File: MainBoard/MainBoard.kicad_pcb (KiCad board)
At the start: 6 copper layers, 45 x 44 mm, 110 parts, among them J2 USB4110-GF-A, J3 M55-7104042R, J4 Conn_01x04_Pin, J5 Conn_01x02_Pin, Q1 PMV19XNEAR, Q2 PMV19XNEAR, Q3 PMV19XNEAR, Q4 PMV19XNEAR, SW1 SW_TL1015AF160QG, SW2 SW_TL1015AF160QG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

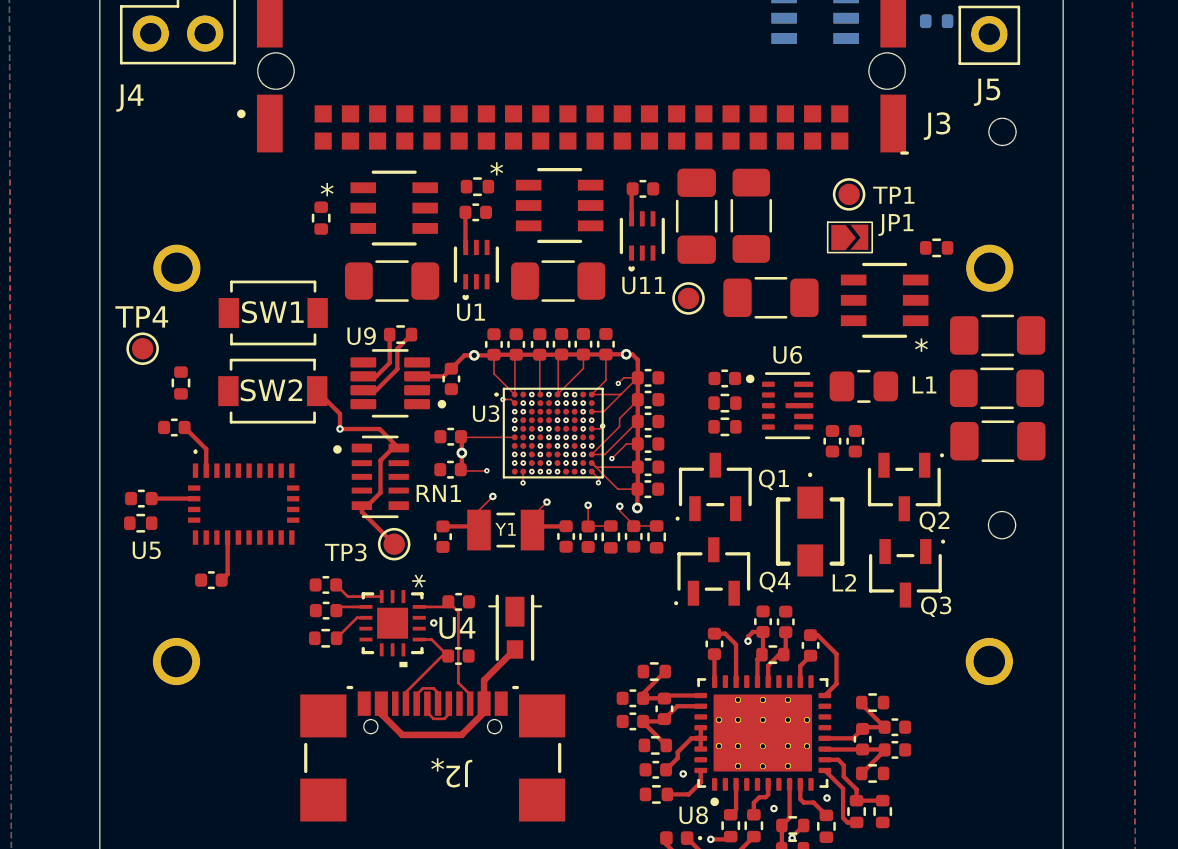
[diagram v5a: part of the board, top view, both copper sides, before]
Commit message: Routed a bunch of stuff
Most if not all fill zones are done
Most if not all cap to 3.3V are done
To start working on communication
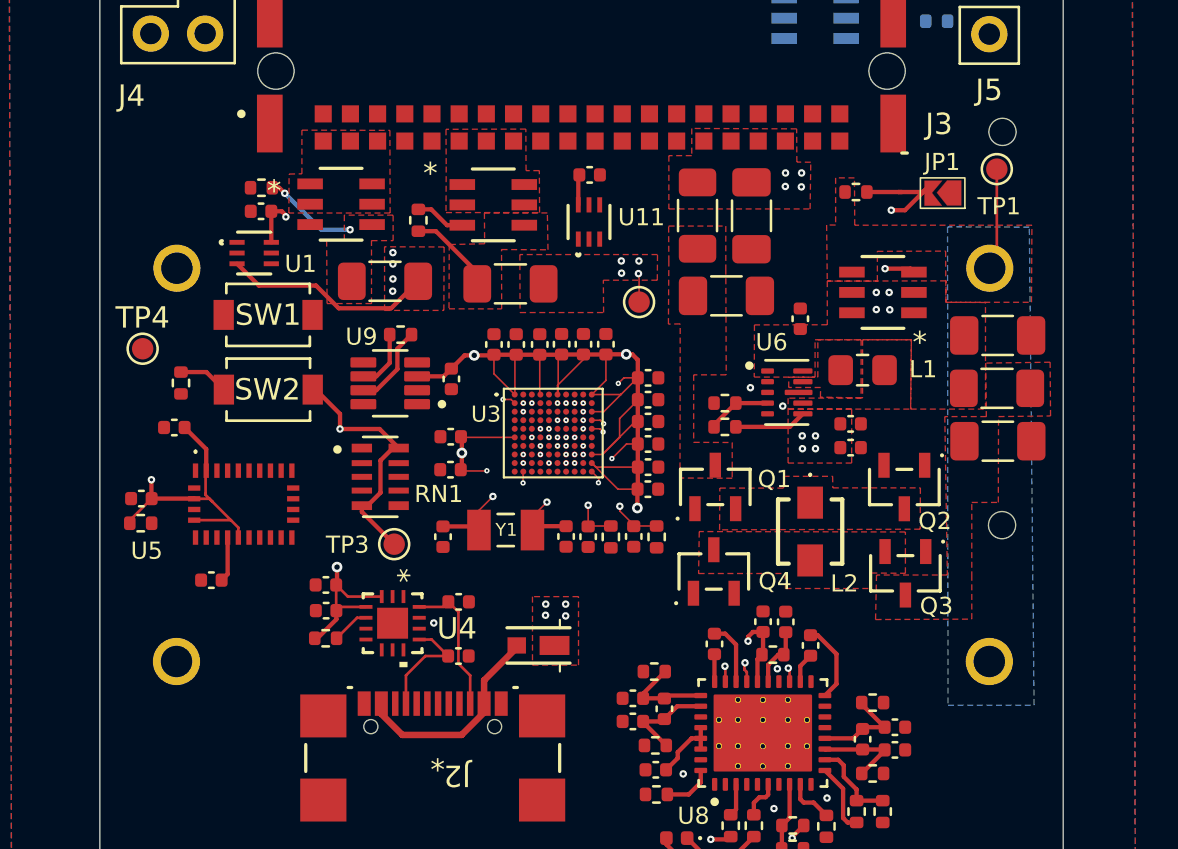
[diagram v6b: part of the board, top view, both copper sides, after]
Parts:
- moved U1 10.4 mm to (76.6, 56.9), turned to 0 degrees
- moved C3 10.0 mm to (76.9, 54.9), turned to 0 degrees
- moved TP1 7.00 mm to (111.3, 52.9)
- moved JP1 4.84 mm to (108.8, 54.0), turned to 180 degrees
- moved R13 4.59 mm to (104.7, 54.0), turned to 180 degrees
- moved C18 4.50 mm to (102.1, 59.9), turned to 90 degrees
- moved R34 3.18 mm to (84.3, 55.3), turned to 90 degrees
- moved R32 3.13 mm to (77.0, 53.8), turned to 180 degrees
- moved U12 3.10 mm to (87.8, 54.6)
- moved C28 2.57 mm to (92.3, 53.2)
- moved U11 2.57 mm to (92.3, 55.4)
- moved C40 2.56 mm to (99.8, 55.1)
- moved R21 2.51 mm to (97.3, 55.1)
- moved U10 2.49 mm to (80.7, 54.6)
- moved TP2 2.32 mm to (94.6, 59.1)
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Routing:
- net +3.3V: track 83.9 -> 110.4 mm, vias 12 -> 23
- net BAT_PULLDOWN: track 0.00 -> 11.5 mm, vias 1 -> 3
- net Net-(U7-S): track 0.00 -> 4.77 mm
- net Net-(U1-IN-): track 0.00 -> 4.44 mm, vias 0 -> 2
- net Net-(U11-IN-): track 0.00 -> 4.08 mm
- net Net-(U6-FB): track 0.00 -> 3.01 mm
- net Net-(U3A-PC14-OSC32_IN): track 8.94 -> 11.4 mm
- net EXTERNAL_BAT_CUTOFF: track 0.00 -> 2.36 mm
- net BOOT0: track 0.00 -> 2.34 mm
- net USB_D-: track 2.13 -> 0.00 mm, vias 1 -> 0
- net USB_D+: track 2.13 -> 0.00 mm, vias 1 -> 0
- net BAT+: track 0.00 -> 1.32 mm, vias 0 -> 8
- net EXTERNAL_LOW_SIDE_DRIVE: track 0.00 -> 0.94 mm, vias 0 -> 1
- net EXTERNAL_HIGH_SIDE_DRIVE: track 0.00 -> 0.73 mm, vias 0 -> 1
- net BAT_LOW_SIDE_DRIVE: track 0.00 -> 0.65 mm, vias 0 -> 1
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- added copper zone on F.Cu, net +3.3V
- added copper zone on F.Cu, net BAT+
- added copper zone on In2.Cu, net BAT+
- added copper zone on In3.Cu, net BAT+
- added copper zone on F.Cu, net BAT_SIDE_INDUC
- added copper zone on F.Cu, net BOARD_OUT_3.3V
- added copper zone on F.Cu, net BOARD_OUT_BAT
- added copper zone on F.Cu, net EXTERNAL_SIDE_INDUC
- added copper zone on F.Cu, net EXTERNAL_VOLTAGE
- added copper zone on In3.Cu, net EXTERNAL_VOLTAGE
- added copper zone on F.Cu, net Net-(Q1-D)
- added copper zone on F.Cu, net Net-(Q3-D)
- added copper zone on F.Cu, net Net-(U1-IN-)
- added copper zone on F.Cu, net Net-(U11-IN-)
- added copper zone on F.Cu, net Net-(U6-L1)
- added copper zone on F.Cu, net Net-(U6-L2)
- added copper zone on B.Cu, net Net-(U7-S)
- added copper zone on F.Cu, net Net-(U7-S)

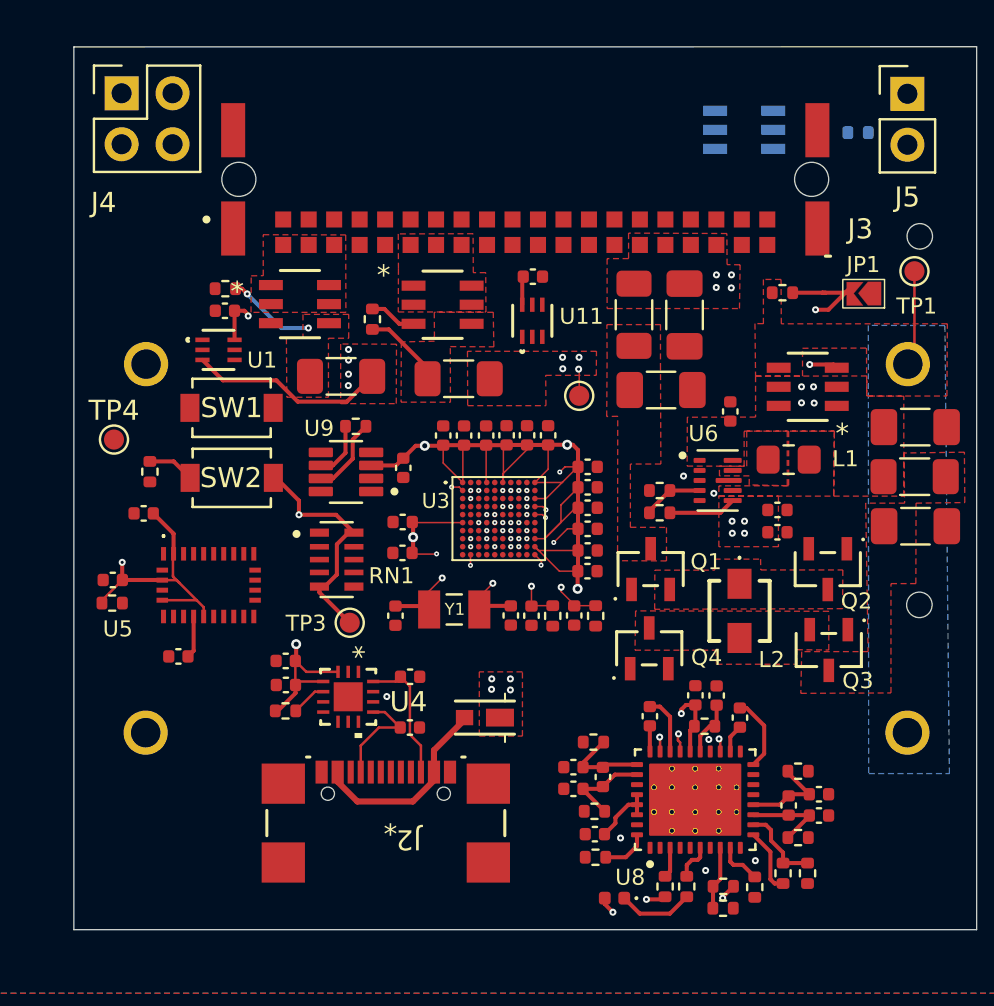
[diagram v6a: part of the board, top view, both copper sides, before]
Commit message: Changes to USB and routing
Added ESD protection IC
Routed USB Differential to STM
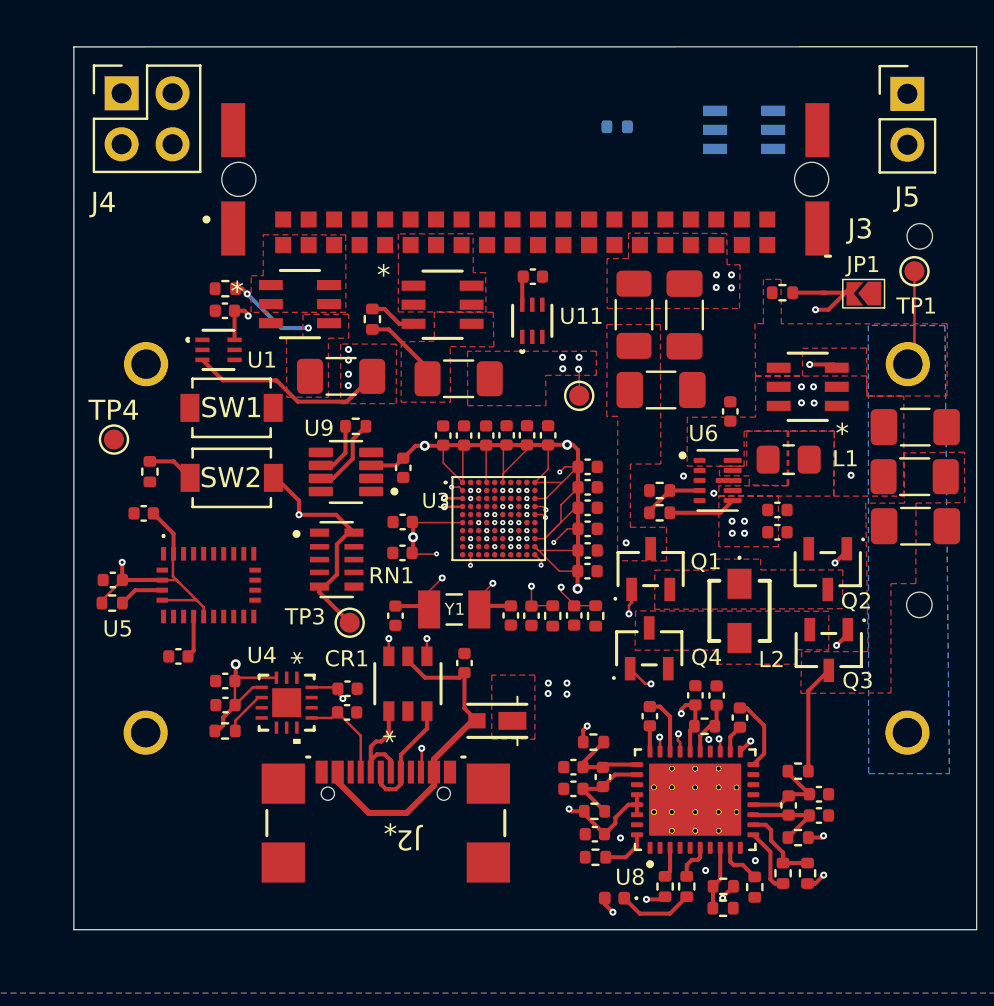
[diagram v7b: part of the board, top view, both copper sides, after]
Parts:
- added C47: 100nF, Capacitor_SMD:C_0402_1005Metric, F.Cu at (88.9, 72.5)
- added CR1: USBLC6-2SC6, inspirefly:SOT23-6L_STM, F.Cu at (86.0, 73.5)
- moved R35 12.0 mm to (96.5, 45.7)
- moved C7 3.22 mm to (83.0, 74.9)
- moved C6 3.18 mm to (83.0, 73.8)
- moved C2 3.17 mm to (77.0, 74.6)
- moved C1 3.17 mm to (76.9, 73.4)
- moved R8 3.17 mm to (76.9, 75.9)
- moved U4 3.08 mm to (80.0, 74.4)
- moved D1 0.64 mm to (90.5, 75.3)
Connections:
- J2 pad A6: USB_D+ -> Net-(J2-DP1)
- J2 pad A7: USB_D- -> Net-(J2-DN1)
- J2 pad B6: USB_D+ -> Net-(J2-DP1)
- J2 pad B7: USB_D- -> Net-(J2-DN1)
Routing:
- net BAT+: track 1.32 -> 24.0 mm, vias 8 -> 11
- net EXTERNAL_LOW_SIDE_DRIVE: track 0.94 -> 13.6 mm, vias 1 -> 2
- net USB_D+: track 0.00 -> 11.5 mm, vias 0 -> 2
- net Net-(Q1-D): track 0.00 -> 10.8 mm, vias 0 -> 2
- net USB_D-: track 0.00 -> 10.1 mm, vias 0 -> 2
- net BAT_HIGH_SIDE_DRIVE: track 0.00 -> 8.33 mm, vias 0 -> 2
- net EXTERNAL_HIGH_SIDE_DRIVE: track 0.73 -> 8.77 mm, vias 1 -> 2
- net Net-(D1-A): track 9.66 -> 16.9 mm
- net EXTERNAL_VOLTAGE: track 3.39 -> 10.2 mm, vias 8 -> 9
- net Net-(J2-DP1): track 0.00 -> 5.99 mm
- net Net-(J2-DN1): track 0.00 -> 5.99 mm
- net BAT_LOW_SIDE_DRIVE: track 0.65 -> 6.53 mm, vias 1 -> 2
- net Net-(Q3-D): track 0.00 -> 5.45 mm
- net IMU_BOOTN: track 0.00 -> 2.25 mm
- net Net-(J2-CC2): track 6.63 -> 8.26 mm, vias 0 -> 2
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
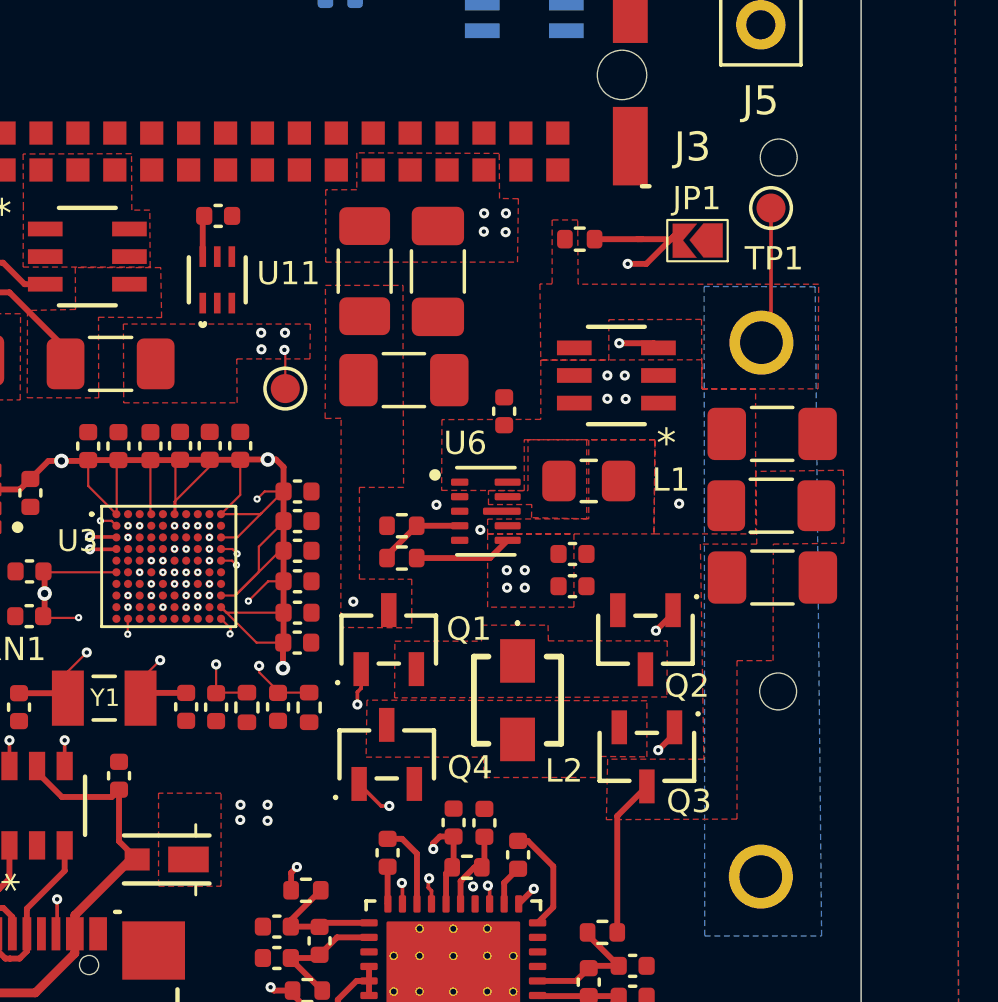
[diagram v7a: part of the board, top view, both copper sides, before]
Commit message: Added E-Fuse/ battery protection IC
Added and routed new IC for battery

- will have to figure out cutoff but that can be done later imo
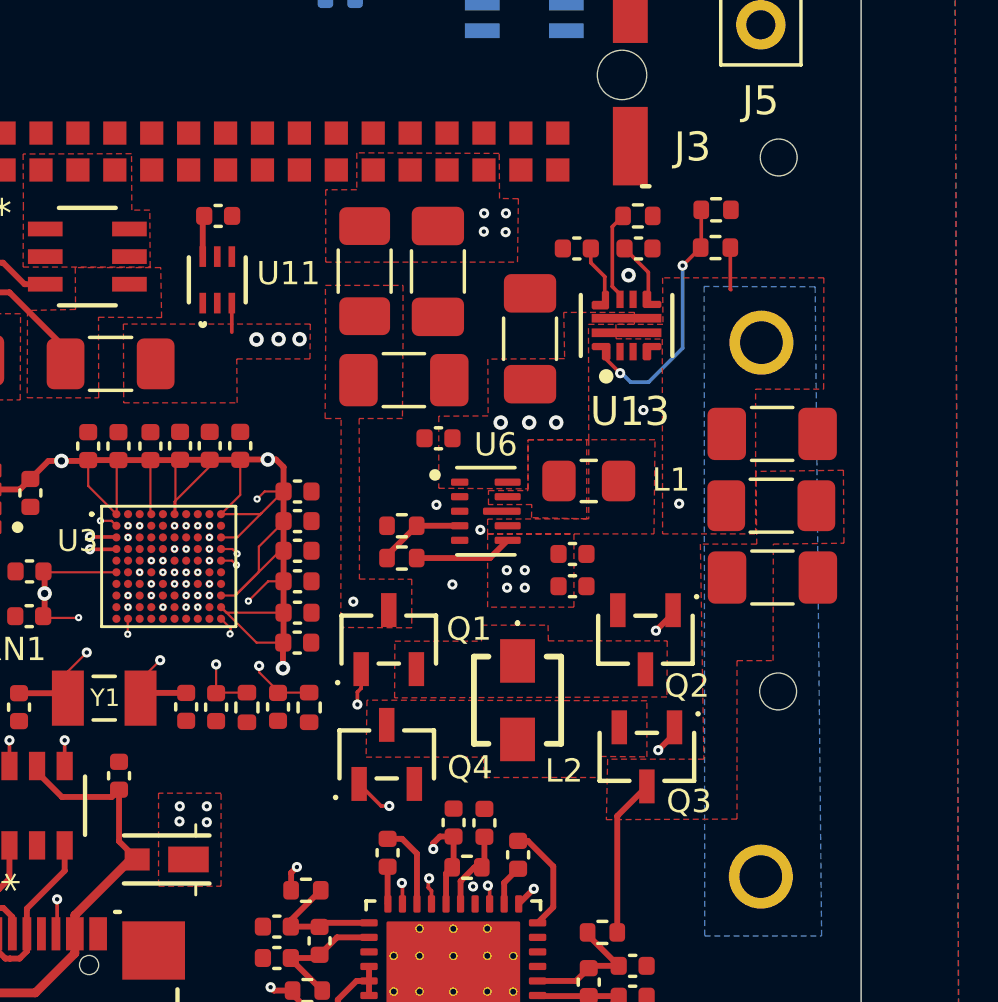
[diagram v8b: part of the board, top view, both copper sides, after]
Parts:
- removed JP1: Footswitch_Disable, inspirefly:SmallJumper
- removed R13: 100K, Resistor_SMD:R_0402_1005Metric
- removed TP1: BatBeforeCutoff, TestPoint:TestPoint_Pad_D1.0mm
- removed TP2: Bat+, TestPoint:TestPoint_Pad_D1.0mm
- removed U7: SI3477DV-T1-GE3, inspirefly:SOT_V-T1-GE3_VIS-M
- added C48: 10nF, Capacitor_SMD:C_0402_1005Metric, F.Cu at (104.6, 54.3)
- added C49: 10nF, Capacitor_SMD:C_0402_1005Metric, F.Cu at (106.7, 54.3)
- added C50: 47uF, Capacitor_SMD:C_1206_3216Metric_Pad1.33x1.80mm_HandSolder, F.Cu at (103.0, 57.4)
- added R3: 143k, Resistor_SMD:R_0402_1005Metric, F.Cu at (109.4, 54.3)
- added R4: 100k, Resistor_SMD:R_0402_1005Metric, F.Cu at (109.4, 53.0)
- added R5: 1k, Resistor_SMD:R_0402_1005Metric, F.Cu at (106.7, 53.2)
- added U13: TPS259472ARPWR, inspirefly:RPW0010A-MFG, F.Cu at (106.3, 57.0)
- moved C18 2.44 mm to (99.9, 60.9), turned to 180 degrees
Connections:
- BT1 pad P: Net-(U7-S) -> BAT+
- BT2 pad P: Net-(U7-S) -> BAT+
- C18 pad 1: BAT+ -> PROTECTED_VOLTAGE
- R33 pad 1: BAT+ -> PROTECTED_VOLTAGE
- R35 pad 2: BAT+ -> PROTECTED_VOLTAGE
- U11 pad 3: BAT+ -> PROTECTED_VOLTAGE
- U2 pad 4: BAT+ -> PROTECTED_VOLTAGE
- U6 pad 1: BAT+ -> PROTECTED_VOLTAGE
- U6 pad 10: BAT+ -> PROTECTED_VOLTAGE
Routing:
- net BAT_PULLDOWN: track 11.5 -> 0.00 mm, vias 3 -> 1
- net Net-(U13-EN_UVLO): track 0.00 -> 8.88 mm, vias 0 -> 2
- net Net-(U7-S): track 4.77 -> 0.00 mm
- net Net-(U13-ILM): track 0.00 -> 3.13 mm
- net EXTERNAL_VOLTAGE: track 10.2 -> 12.9 mm
- net Net-(U13-dVdt): track 0.00 -> 2.24 mm
- net Net-(U13-ITIMER): track 0.00 -> 2.10 mm
- net PROTECTED_VOLTAGE: track 0.00 -> 1.00 mm, vias 0 -> 6
- net BAT+: track 24.0 -> 24.1 mm, vias 11 -> 3
- net GND: vias 12 -> 15
- added copper zone on B.Cu, net BAT+
- added copper zone on F.Cu, net PROTECTED_VOLTAGE
- added copper zone on In3.Cu, net PROTECTED_VOLTAGE
- removed copper zone on In2.Cu, net BAT+
- removed copper zone on In3.Cu, net BAT+
- removed copper zone on B.Cu, net Net-(U7-S)
- removed copper zone on F.Cu, net Net-(U7-S)
